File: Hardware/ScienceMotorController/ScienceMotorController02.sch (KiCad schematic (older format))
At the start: 1 part, among them U1 TM4C129E_Launchpad

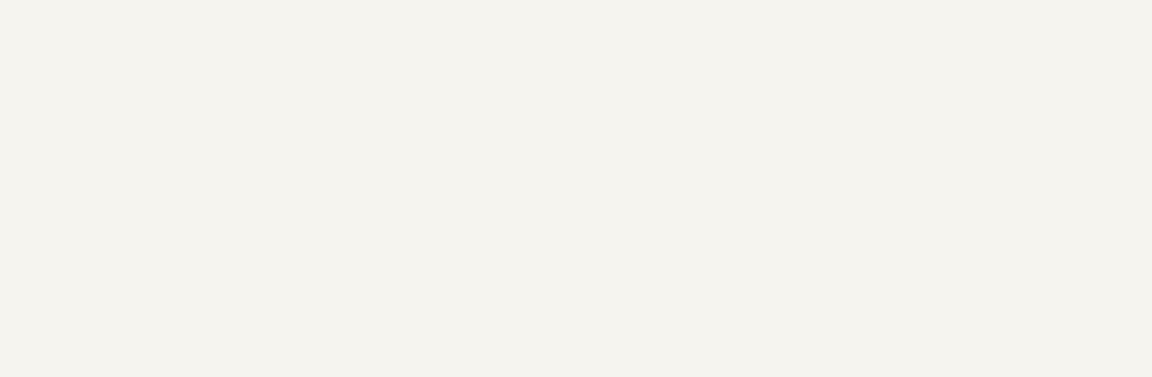
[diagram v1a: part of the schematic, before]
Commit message: Sheet titles
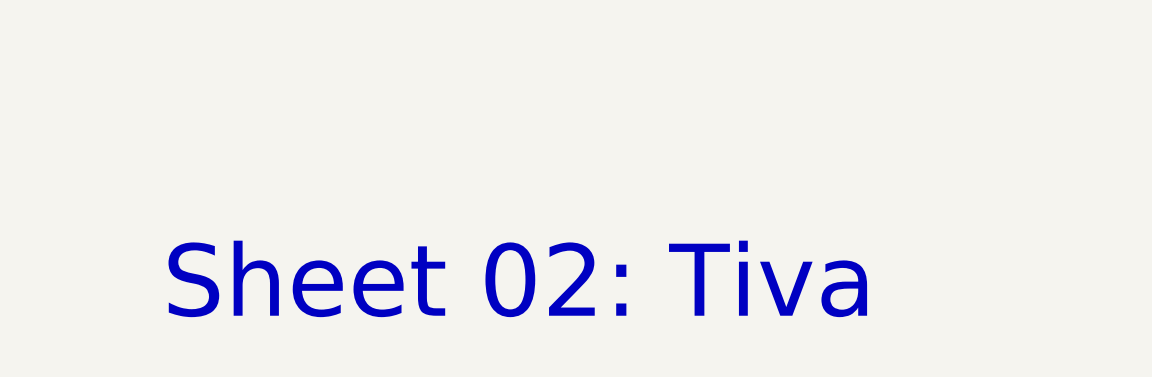
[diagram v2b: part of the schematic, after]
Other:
- note added: "Sheet 02: Tiva"
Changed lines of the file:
@@
 $Descr A4 11693 8268
 encoding utf-8
-Sheet 3 10
+Sheet 3 11
 Title ""
 Date ""
@@
 Text Notes 8450 2450 0    79   ~ 0
 PWM Pins are:\nPF_1, PF_2, PF_3, PF_0\nPG_1, PK_4, PK_5
+Text Notes 7350 7000 0    315  ~ 0
+Sheet 02: Tiva
 $EndSCHEMATC

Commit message: Flagged Tiva
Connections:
- net +3V3: now reaches U1.+3V3 (A1_1)
- net +3V3: now also U1.+3V3' (A2_1)
- net Limit_Switch_2: now reaches U1.PA6 (B1_8)
- net Limit_Switch_1: now reaches U1.PD7 (B1_7)
- net Limit_Switch_3: now reaches U1.PM4 (B1_9)
- net Limit_Switch_4: now reaches U1.PM5 (B1_10)
- net PWM_1: now reaches U1.PF1 (C1_1)
- net PWM_2: now reaches U1.PF2 (C1_2)
- net PWM_3: now reaches U1.PF3 (C1_3)
- net Current_Sense_1: now reaches U1.PB4 (B2_3)
- net Current_Sense_2: now reaches U1.PB5 (B2_4)
- net Current_Sense_3: now reaches U1.PK0 (B2_5)
- net Current_Sense_4: now reaches U1.PK1 (B2_6)
- net Current_Sense_5: now reaches U1.PK2 (B2_7)
- net Current_Sense_6: now reaches U1.PK3 (B2_8)
- net PWM_4: now reaches U1.PG1 (C2_1)
- net PWM_5: now reaches U1.PK4 (C2_2)
- net PWM_6: now reaches U1.PK5 (C2_3)
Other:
- note added: "Analog Read Pins used are:\nPB_4, PB_5, PK_0, \nPK_1, PK_2, PK_3"
- note added: "PWM Pins used are:\nPF_1, PF_2, PF_3, \nPG_1, PK_4, PK_5"
- note removed: "PWM Pins are:\nPF_1, PF_2, PF_3, PF_0\nPG_1, PK_4, PK_5"
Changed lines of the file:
@@
 U 1 1 5F715123
 P 4200 3200
-F 0 "U1" H 4300 4450 60  0000 L CNN
-F 1 "TM4C129E_Launchpad" H 3500 4350 60  0000 L CNN
+F 0 "U1" H 4300 4600 60  0000 L CNN
+F 1 "TM4C129E_Launchpad" H 3500 4500 60  0000 L CNN
 F 2 "" H 4200 3200 60  0001 C CNN
 F 3 "" H 4200 3200 60  0001 C CNN
@@
 U 2 1 5F716DA0
 P 4800 3200
-F 0 "U1" H 5000 4450 60  0000 C CNN
-F 1 "TM4C129E_Launchpad" H 4600 4350 60  0000 C CNN
+F 0 "U1" H 5000 4600 60  0000 C CNN
+F 1 "TM4C129E_Launchpad" H 4600 4500 60  0000 C CNN
 F 2 "" H 4800 3200 60  0001 C CNN
 F 3 "" H 4800 3200 60  0001 C CNN
@@
 U 3 1 5F7264AA
 P 6350 3200
-F 0 "U1" H 6450 4450 60  0000 L CNN
-F 1 "TM4C129E_Launchpad" H 5700 4350 60  0000 L CNN
+F 0 "U1" H 6450 4600 60  0000 L CNN
+F 1 "TM4C129E_Launchpad" H 5700 4500 60  0000 L CNN
 F 2 "" H 6350 3200 60  0001 C CNN
 F 3 "" H 6350 3200 60  0001 C CNN
@@
 U 4 1 5F72B226
 P 6950 3200
-F 0 "U1" H 7100 4450 60  0000 C CNN
-F 1 "TM4C129E_Launchpad" H 6700 4350 60  0000 C CNN
+F 0 "U1" H 7100 4600 60  0000 C CNN
+F 1 "TM4C129E_Launchpad" H 6700 4500 60  0000 C CNN
 F 2 "" H 6950 3200 60  0001 C CNN
 F 3 "" H 6950 3200 60  0001 C CNN
@@
 U 5 1 5F733DC7
 P 4200 4700
-F 0 "U1" H 4300 5950 60  0000 L CNN
-F 1 "TM4C129E_Launchpad" H 3500 5850 60  0000 L CNN
+F 0 "U1" H 4300 6050 60  0000 L CNN
+F 1 "TM4C129E_Launchpad" H 3500 5950 60  0000 L CNN
 F 2 "" H 4200 4700 60  0001 C CNN
 F 3 "" H 4200 4700 60  0001 C CNN
@@
 U 6 1 5F73B2DD
 P 4800 4700
-F 0 "U1" H 5000 5950 60  0000 C CNN
-F 1 "TM4C129E_Launchpad" H 4600 5850 60  0000 C CNN
+F 0 "U1" H 5000 6050 60  0000 C CNN
+F 1 "TM4C129E_Launchpad" H 4600 5950 60  0000 C CNN
 F 2 "" H 4800 4700 60  0001 C CNN
 F 3 "" H 4800 4700 60  0001 C CNN
@@
 U 7 1 5F740CF4
 P 6350 4700
-F 0 "U1" H 6450 5950 60  0000 L CNN
-F 1 "TM4C129E_Launchpad" H 5650 5850 60  0000 L CNN
+F 0 "U1" H 6450 6050 60  0000 L CNN
+F 1 "TM4C129E_Launchpad" H 5650 5950 60  0000 L CNN
 F 2 "" H 6350 4700 60  0001 C CNN
 F 3 "" H 6350 4700 60  0001 C CNN
@@
 U 8 1 5F7529E8
 P 6950 4700
-F 0 "U1" H 7100 5950 60  0000 C CNN
-F 1 "TM4C129E_Launchpad" H 6700 5850 60  0000 C CNN
+F 0 "U1" H 7100 6050 60  0000 C CNN
+F 1 "TM4C129E_Launchpad" H 6700 5950 60  0000 C CNN
 F 2 "" H 6950 4700 60  0001 C CNN
 F 3 "" H 6950 4700 60  0001 C CNN
@@
 $EndComp
 Text Notes 8450 2450 0    79   ~ 0
-PWM Pins are:\nPF_1, PF_2, PF_3, PF_0\nPG_1, PK_4, PK_5
+PWM Pins used are:\nPF_1, PF_2, PF_3, \nPG_1, PK_4, PK_5
+Text GLabel 6000 2250 0    39   Output ~ 0
+PWM_1
+Wire Wire Line
+	6000 2250 6150 2250
+Text GLabel 6000 2350 0    39   Output ~ 0
+PWM_2
+Wire Wire Line
+	6150 2350 6000 2350
+Text GLabel 6000 2450 0    39   Output ~ 0
+PWM_3
+Wire Wire Line
+	6000 2450 6150 2450
+Wire Wire Line
+	4000 2250 3850 2250
+Wire Wire Line
+	3850 2250 3850 2200
+$Comp
+L power:+3.3V #PWR?
+U 1 1 5FB06302
+P 3850 2200
+F 0 "#PWR?" H 3850 2050 50  0001 C CNN
+F 1 "+3.3V" H 3865 2373 50  0000 C CNN
+F 2 "" H 3850 2200 50  0001 C CNN
+F 3 "" H 3850 2200 50  0001 C CNN
+	1    3850 2200
+	1    0    0    -1
+$EndComp
+Text GLabel 6000 3750 0    39   Output ~ 0
+PWM_4
+Text GLabel 6000 3850 0    39   Output ~ 0
+PWM_5
+Text GLabel 6000 3950 0    39   Output ~ 0
+PWM_6
+Wire Wire Line
+	6000 3750 6150 3750
+Wire Wire Line
+	6150 3850 6000 3850
+Wire Wire Line
+	6150 3950 6000 3950
+Text Notes 8450 2950 0    79   ~ 0
+Analog Read Pins used are:\nPB_4, PB_5, PK_0, \nPK_1, PK_2, PK_3
+Text GLabel 5100 3950 2    39   Input ~ 0
+Current_Sense_1
+Wire Wire Line
+	5100 3950 5000 3950
+Wire Wire Line
+	5000 4050 5100 4050
+Wire Wire Line
+	5000 4150 5100 4150
+Wire Wire Line
+	5000 4250 5100 4250
+Wire Wire Line
+	5000 4350 5100 4350
+Wire Wire Line
+	5000 4450 5100 4450
+Text GLabel 5100 4050 2    39   Input ~ 0
+Current_Sense_2
+Text GLabel 5100 4150 2    39   Input ~ 0
+Current_Sense_3
+Text GLabel 5100 4250 2    39   Input ~ 0
+Current_Sense_4
+Text GLabel 5100 4350 2    39   Input ~ 0
+Current_Sense_5
+Text GLabel 5100 4450 2    39   Input ~ 0
+Current_Sense_6
+$Comp
+L power:+3.3V #PWR?
+U 1 1 5FB0EFA7
+P 3850 3700
+F 0 "#PWR?" H 3850 3550 50  0001 C CNN
+F 1 "+3.3V" H 3865 3873 50  0000 C CNN
+F 2 "" H 3850 3700 50  0001 C CNN
+F 3 "" H 3850 3700 50  0001 C CNN
+	1    3850 3700
+	1    0    0    -1
+$EndComp
+Wire Wire Line
+	3850 3700 3850 3750
+Wire Wire Line
+	3850 3750 4000 3750
+Text GLabel 5100 2850 2    39   Input ~ 0
+Limit_Switch_1
+Wire Wire Line
+	5100 2850 5000 2850
+Text GLabel 5100 2950 2    39   Input ~ 0
+Limit_Switch_2
+Text GLabel 5100 3050 2    39   Input ~ 0
+Limit_Switch_3
+Text GLabel 5100 3150 2    39   Input ~ 0
+Limit_Switch_4
+Wire Wire Line
+	5100 2950 5000 2950
+Wire Wire Line
+	5000 3050 5100 3050
+Wire Wire Line
+	5100 3150 5000 3150
 Text Notes 7350 7000 0    315  ~ 0
 Sheet 02: Tiva

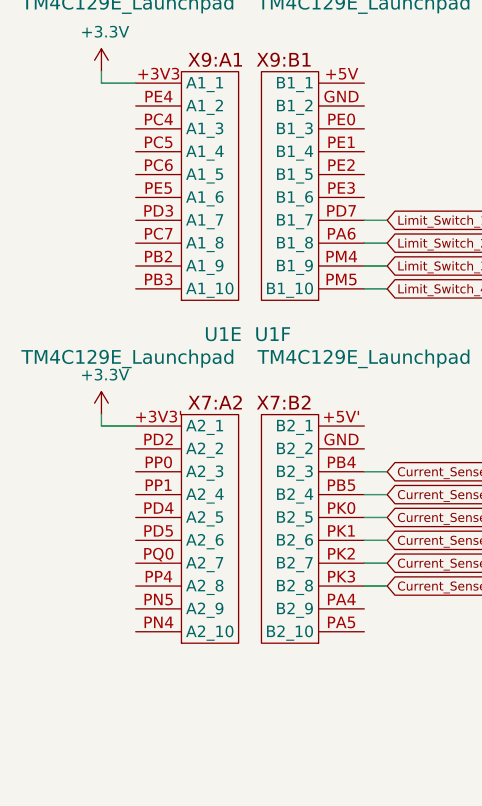
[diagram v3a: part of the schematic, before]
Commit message: changed everything to actuation, added schottky diode, added A/B flags to tiva
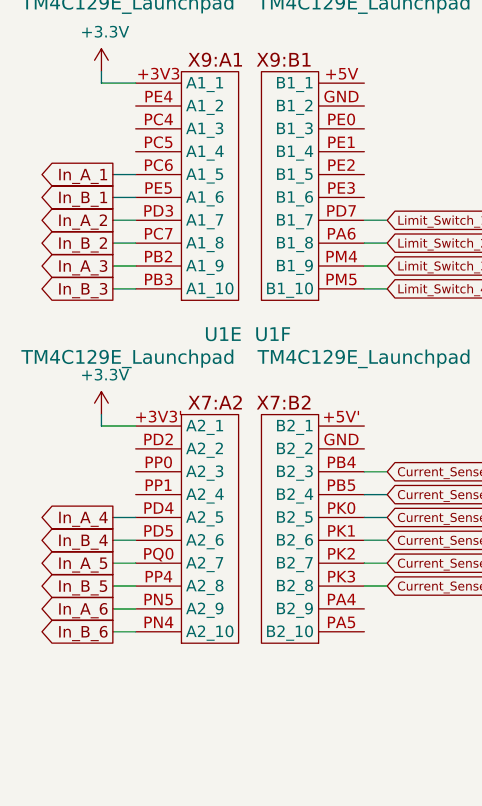
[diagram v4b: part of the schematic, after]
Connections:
- net In_A_3: now reaches U1.PB2 (A1_9)
- net In_B_3: now reaches U1.PB3 (A1_10)
- net In_A_1: now reaches U1.PC6 (A1_5)
- net In_B_2: now reaches U1.PC7 (A1_8)
- net In_A_2: now reaches U1.PD3 (A1_7)
- net In_B_1: now reaches U1.PE5 (A1_6)
- net In_A_4: now reaches U1.PD4 (A2_5)
- net In_B_4: now reaches U1.PD5 (A2_6)
- net In_B_6: now reaches U1.PN4 (A2_10)
- net In_A_6: now reaches U1.PN5 (A2_9)
- net In_B_5: now reaches U1.PP4 (A2_8)
- net In_A_5: now reaches U1.PQ0 (A2_7)
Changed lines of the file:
@@
 Text Notes 7350 7000 0    315  ~ 0
 Sheet 02: Tiva
+Text GLabel 3900 2650 0    50   Output ~ 0
+In_A_1
+Wire Wire Line
+	4000 2650 3900 2650
+Text GLabel 3900 2750 0    50   Output ~ 0
+In_B_1
+Wire Wire Line
+	4000 2750 3900 2750
+Text GLabel 3900 2850 0    50   Output ~ 0
+In_A_2
+Text GLabel 3900 2950 0    50   Output ~ 0
+In_B_2
+Text GLabel 3900 3050 0    50   Output ~ 0
+In_A_3
+Text GLabel 3900 4150 0    50   Output ~ 0
+In_A_4
+Text GLabel 3900 3150 0    50   Output ~ 0
+In_B_3
+Text GLabel 3900 4250 0    50   Output ~ 0
+In_B_4
+Text GLabel 3900 4350 0    50   Output ~ 0
+In_A_5
+Text GLabel 3900 4450 0    50   Output ~ 0
+In_B_5
+Text GLabel 3900 4550 0    50   Output ~ 0
+In_A_6
+Text GLabel 3900 4650 0    50   Output ~ 0
+In_B_6
+Wire Wire Line
+	4000 2850 3900 2850
+Wire Wire Line
+	3900 2950 4000 2950
+Wire Wire Line
+	4000 3050 3900 3050
+Wire Wire Line
+	4000 3150 3900 3150
+Wire Wire Line
+	3900 4150 4000 4150
+Wire Wire Line
+	4000 4250 3900 4250
+Wire Wire Line
+	3900 4350 4000 4350
+Wire Wire Line
+	4000 4450 3900 4450
+Wire Wire Line
+	3900 4550 4000 4550
+Wire Wire Line
+	4000 4650 3900 4650
 $EndSCHEMATC

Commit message: added ferrite beads
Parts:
- added D?: Yellow, symbol Device:LED
- added D?: Red, symbol Device:LED
- added R? (x2): 330, symbol Device:R
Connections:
- net at U1.PM6 (D2_10): now also R?.1
- net at U1.PP3 (D2_8): now also R?.1
- net +3V3 renamed +3.3VA
- new net: D?.2 (A), R?.2 (x2)
- new net GND: D?.1 (K), D?.1 (K)
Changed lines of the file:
@@
 Wire Wire Line
 	3850 2250 3850 2200
-$Comp
-L power:+3.3V #PWR?
-U 1 1 5FB06302
-P 3850 2200
-F 0 "#PWR?" H 3850 2050 50  0001 C CNN
-F 1 "+3.3V" H 3865 2373 50  0000 C CNN
-F 2 "" H 3850 2200 50  0001 C CNN
-F 3 "" H 3850 2200 50  0001 C CNN
-	1    3850 2200
-	1    0    0    -1
-$EndComp
 Text GLabel 6000 3750 0    39   Output ~ 0
 PWM_4
@@
 Text GLabel 5100 4450 2    39   Input ~ 0
 Current_Sense_6
-$Comp
-L power:+3.3V #PWR?
-U 1 1 5FB0EFA7
-P 3850 3700
-F 0 "#PWR?" H 3850 3550 50  0001 C CNN
-F 1 "+3.3V" H 3865 3873 50  0000 C CNN
-F 2 "" H 3850 3700 50  0001 C CNN
-F 3 "" H 3850 3700 50  0001 C CNN
-	1    3850 3700
-	1    0    0    -1
-$EndComp
 Wire Wire Line
 	3850 3700 3850 3750
@@
 Wire Wire Line
 	4000 4650 3900 4650
+$Comp
+L power:+3.3VA #PWR?
+U 1 1 5F8320C1
+P 3850 2200
+F 0 "#PWR?" H 3850 2050 50  0001 C CNN
+F 1 "+3.3VA" H 3865 2373 50  0000 C CNN
+F 2 "" H 3850 2200 50  0001 C CNN
+F 3 "" H 3850 2200 50  0001 C CNN
+	1    3850 2200
+	1    0    0    -1
+$EndComp
+$Comp
+L power:+3.3VA #PWR?
+U 1 1 5F833369
+P 3850 3700
+F 0 "#PWR?" H 3850 3550 50  0001 C CNN
+F 1 "+3.3VA" H 3865 3873 50  0000 C CNN
+F 2 "" H 3850 3700 50  0001 C CNN
+F 3 "" H 3850 3700 50  0001 C CNN
+	1    3850 3700
+	1    0    0    -1
+$EndComp
+Wire Wire Line
+	7150 4650 7250 4650
+$Comp
+L Device:R R?
+U 1 1 5F836CF2
+P 7400 4650
+F 0 "R?" V 7300 4650 50  0000 C CNN
+F 1 "330" V 7400 4650 50  0000 C CNN
+F 2 "" V 7330 4650 50  0001 C CNN
+F 3 "~" H 7400 4650 50  0001 C CNN
+	1    7400 4650
+	0    -1   -1   0
+$EndComp
+$Comp
+L Device:LED D?
+U 1 1 5F838880
+P 7800 4650
+F 0 "D?" H 7800 4750 50  0000 C CNN
+F 1 "Yellow" H 7600 4700 50  0000 C CNN
+F 2 "" H 7800 4650 50  0001 C CNN
+F 3 "~" H 7800 4650 50  0001 C CNN
+	1    7800 4650
+	-1   0    0    1
+$EndComp
+Wire Wire Line
+	7550 4650 7650 4650
+Wire Wire Line
+	7950 4650 8250 4650
+$Comp
+L power:GND #PWR?
+U 1 1 5F83BC3E
+P 8250 4650
+F 0 "#PWR?" H 8250 4400 50  0001 C CNN
+F 1 "GND" V 8255 4522 50  0000 R CNN
+F 2 "" H 8250 4650 50  0001 C CNN
+F 3 "" H 8250 4650 50  0001 C CNN
+	1    8250 4650
+	0    -1   -1   0
+$EndComp
+$Comp
+L Device:R R?
+U 1 1 5F83D1F8
+P 7400 4450
+F 0 "R?" V 7300 4450 50  0000 C CNN
+F 1 "330" V 7400 4450 50  0000 C CNN
+F 2 "" V 7330 4450 50  0001 C CNN
+F 3 "~" H 7400 4450 50  0001 C CNN
+	1    7400 4450
+	0    -1   -1   0
+$EndComp
+$Comp
+L Device:LED D?
+U 1 1 5F83D4EA
+P 7800 4450
+F 0 "D?" H 7800 4550 50  0000 C CNN
+F 1 "Red" H 7650 4500 50  0000 C CNN
+F 2 "" H 7800 4450 50  0001 C CNN
+F 3 "~" H 7800 4450 50  0001 C CNN
+	1    7800 4450
+	-1   0    0    1
+$EndComp
+$Comp
+L power:GND #PWR?
+U 1 1 5F83E3D5
+P 8250 4450
+F 0 "#PWR?" H 8250 4200 50  0001 C CNN
+F 1 "GND" V 8255 4322 50  0000 R CNN
+F 2 "" H 8250 4450 50  0001 C CNN
+F 3 "" H 8250 4450 50  0001 C CNN
+	1    8250 4450
+	0    -1   -1   0
+$EndComp
+Wire Wire Line
+	8250 4450 7950 4450
+Wire Wire Line
+	7650 4450 7550 4450
+Wire Wire Line
+	7250 4450 7150 4450
 $EndSCHEMATC

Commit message: schematic review
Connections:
- net GND: now also U1.GND (B1_2), U1.GND (B2_2), U1.GND (D1_1), U1.GND (D2_1)
- net +3.3VA renamed 3.3VA
- no-connect marks 0 -> 44
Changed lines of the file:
@@
 $Descr A4 11693 8268
 encoding utf-8
-Sheet 3 11
+Sheet 3 10
 Title ""
 Date ""
@@
 U 1 1 5F715123
 P 4200 3200
-F 0 "U1" H 4300 4600 60  0000 L CNN
-F 1 "TM4C129E_Launchpad" H 3500 4500 60  0000 L CNN
+F 0 "U1" H 4300 4700 60  0000 L CNN
+F 1 "TM4C129E_Launchpad" H 3500 4600 60  0000 L CNN
 F 2 "" H 4200 3200 60  0001 C CNN
 F 3 "" H 4200 3200 60  0001 C CNN
@@
 U 2 1 5F716DA0
 P 4800 3200
-F 0 "U1" H 5000 4600 60  0000 C CNN
-F 1 "TM4C129E_Launchpad" H 4600 4500 60  0000 C CNN
+F 0 "U1" H 5000 4700 60  0000 C CNN
+F 1 "TM4C129E_Launchpad" H 4600 4600 60  0000 C CNN
 F 2 "" H 4800 3200 60  0001 C CNN
 F 3 "" H 4800 3200 60  0001 C CNN
@@
 U 5 1 5F733DC7
 P 4200 4700
-F 0 "U1" H 4300 6050 60  0000 L CNN
-F 1 "TM4C129E_Launchpad" H 3500 5950 60  0000 L CNN
+F 0 "U1" H 4300 6100 60  0000 L CNN
+F 1 "TM4C129E_Launchpad" H 3500 6000 60  0000 L CNN
 F 2 "" H 4200 4700 60  0001 C CNN
 F 3 "" H 4200 4700 60  0001 C CNN
@@
 U 6 1 5F73B2DD
 P 4800 4700
-F 0 "U1" H 5000 6050 60  0000 C CNN
-F 1 "TM4C129E_Launchpad" H 4600 5950 60  0000 C CNN
+F 0 "U1" H 5000 6100 60  0000 C CNN
+F 1 "TM4C129E_Launchpad" H 4600 6000 60  0000 C CNN
 F 2 "" H 4800 4700 60  0001 C CNN
 F 3 "" H 4800 4700 60  0001 C CNN
@@
 Text GLabel 5100 4450 2    39   Input ~ 0
 Current_Sense_6
-Wire Wire Line
-	3850 3700 3850 3750
-Wire Wire Line
-	3850 3750 4000 3750
 Text GLabel 5100 2850 2    39   Input ~ 0
 Limit_Switch_1
@@
 Wire Wire Line
 	4000 4650 3900 4650
-$Comp
-L power:+3.3VA #PWR?
-U 1 1 5F8320C1
-P 3850 2200
-F 0 "#PWR?" H 3850 2050 50  0001 C CNN
-F 1 "+3.3VA" H 3865 2373 50  0000 C CNN
-F 2 "" H 3850 2200 50  0001 C CNN
-F 3 "" H 3850 2200 50  0001 C CNN
-	1    3850 2200
-	1    0    0    -1
-$EndComp
-$Comp
-L power:+3.3VA #PWR?
-U 1 1 5F833369
-P 3850 3700
-F 0 "#PWR?" H 3850 3550 50  0001 C CNN
-F 1 "+3.3VA" H 3865 3873 50  0000 C CNN
-F 2 "" H 3850 3700 50  0001 C CNN
-F 3 "" H 3850 3700 50  0001 C CNN
-	1    3850 3700
-	1    0    0    -1
-$EndComp
 Wire Wire Line
 	7150 4650 7250 4650
@@
 Wire Wire Line
 	7550 4650 7650 4650
-Wire Wire Line
-	7950 4650 8250 4650
 $Comp
 L power:GND #PWR?
 U 1 1 5F83BC3E
-P 8250 4650
-F 0 "#PWR?" H 8250 4400 50  0001 C CNN
-F 1 "GND" V 8255 4522 50  0000 R CNN
-F 2 "" H 8250 4650 50  0001 C CNN
-F 3 "" H 8250 4650 50  0001 C CNN
-	1    8250 4650
-	0    -1   -1   0
+P 8300 4700
+F 0 "#PWR?" H 8300 4450 50  0001 C CNN
+F 1 "GND" H 8550 4650 50  0000 R CNN
+F 2 "" H 8300 4700 50  0001 C CNN
+F 3 "" H 8300 4700 50  0001 C CNN
+	1    8300 4700
+	1    0    0    -1
 $EndComp
 $Comp
@@
 L power:GND #PWR?
 U 1 1 5F83E3D5
-P 8250 4450
-F 0 "#PWR?" H 8250 4200 50  0001 C CNN
-F 1 "GND" V 8255 4322 50  0000 R CNN
-F 2 "" H 8250 4450 50  0001 C CNN
-F 3 "" H 8250 4450 50  0001 C CNN
-	1    8250 4450
-	0    -1   -1   0
-$EndComp
-Wire Wire Line
-	8250 4450 7950 4450
+P 8300 4500
+F 0 "#PWR?" H 8300 4250 50  0001 C CNN
+F 1 "GND" H 8550 4450 50  0000 R CNN
+F 2 "" H 8300 4500 50  0001 C CNN
+F 3 "" H 8300 4500 50  0001 C CNN
+	1    8300 4500
+	1    0    0    -1
+$EndComp
 Wire Wire Line
 	7650 4450 7550 4450
 Wire Wire Line
 	7250 4450 7150 4450
+Wire Wire Line
+	8300 4450 8300 4500
+Wire Wire Line
+	7950 4450 8300 4450
+Wire Wire Line
+	8300 4650 8300 4700
+Wire Wire Line
+	7950 4650 8300 4650
+NoConn ~ 7150 3850
+NoConn ~ 7150 3950
+NoConn ~ 7150 4050
+NoConn ~ 7150 4150
+NoConn ~ 7150 4250
+NoConn ~ 7150 4350
+NoConn ~ 7150 4550
+NoConn ~ 6150 4650
+NoConn ~ 6150 4550
+NoConn ~ 6150 4450
+NoConn ~ 6150 4350
+NoConn ~ 6150 4250
+NoConn ~ 6150 4150
+NoConn ~ 6150 4050
+Wire Wire Line
+	7150 3750 7350 3750
+Wire Wire Line
+	7350 3750 7350 3800
+$Comp
+L power:GND #PWR?
+U 1 1 5F8BF81D
+P 7350 3800
+F 0 "#PWR?" H 7350 3550 50  0001 C CNN
+F 1 "GND" H 7600 3750 50  0000 R CNN
+F 2 "" H 7350 3800 50  0001 C CNN
+F 3 "" H 7350 3800 50  0001 C CNN
+	1    7350 3800
+	1    0    0    -1
+$EndComp
+NoConn ~ 4000 3850
+NoConn ~ 4000 3950
+NoConn ~ 4000 4050
+Wire Wire Line
+	5000 3850 5700 3850
+Wire Wire Line
+	5700 3850 5700 3950
+$Comp
+L power:GND #PWR?
+U 1 1 5F8C3C62
+P 5700 3950
+F 0 "#PWR?" H 5700 3700 50  0001 C CNN
+F 1 "GND" H 5800 3800 50  0000 R CNN
+F 2 "" H 5700 3950 50  0001 C CNN
+F 3 "" H 5700 3950 50  0001 C CNN
+	1    5700 3950
+	1    0    0    -1
+$EndComp
+NoConn ~ 5000 4550
+NoConn ~ 5000 4650
+NoConn ~ 5000 2750
+NoConn ~ 5000 2650
+NoConn ~ 5000 2550
+NoConn ~ 5000 2450
+NoConn ~ 4000 2550
+NoConn ~ 4000 2450
+NoConn ~ 4000 2350
+NoConn ~ 6150 2550
+NoConn ~ 6150 2650
+NoConn ~ 6150 2750
+NoConn ~ 6150 2850
+NoConn ~ 6150 2950
+NoConn ~ 6150 3050
+NoConn ~ 6150 3150
+NoConn ~ 7150 3150
+NoConn ~ 7150 3050
+NoConn ~ 7150 2950
+NoConn ~ 7150 2850
+NoConn ~ 7150 2750
+NoConn ~ 7150 2650
+NoConn ~ 7150 2550
+NoConn ~ 7150 2450
+NoConn ~ 7150 2350
+Wire Wire Line
+	7150 2250 7400 2250
+Wire Wire Line
+	7400 2250 7400 2300
+$Comp
+L power:GND #PWR?
+U 1 1 5F8D9D39
+P 7400 2300
+F 0 "#PWR?" H 7400 2050 50  0001 C CNN
+F 1 "GND" H 7500 2150 50  0000 R CNN
+F 2 "" H 7400 2300 50  0001 C CNN
+F 3 "" H 7400 2300 50  0001 C CNN
+	1    7400 2300
+	1    0    0    -1
+$EndComp
+Wire Wire Line
+	5000 2350 5250 2350
+Wire Wire Line
+	5250 2350 5250 2400
+$Comp
+L power:GND #PWR?
+U 1 1 5F8DBCE3
+P 5250 2400
+F 0 "#PWR?" H 5250 2150 50  0001 C CNN
+F 1 "GND" H 5350 2250 50  0000 R CNN
+F 2 "" H 5250 2400 50  0001 C CNN
+F 3 "" H 5250 2400 50  0001 C CNN
+	1    5250 2400
+	1    0    0    -1
+$EndComp
+NoConn ~ 5000 2250
+NoConn ~ 5000 3750
+Text HLabel 3850 2200 1    50   Input ~ 0
+3.3VA
+Text HLabel 3750 3750 0    50   Input ~ 0
+3.3VA
+Wire Wire Line
+	3750 3750 4000 3750
 $EndSCHEMATC

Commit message: made some more hierarchal changes
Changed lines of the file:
@@
 Wire Wire Line
 	6000 2450 6150 2450
-Wire Wire Line
-	4000 2250 3850 2250
-Wire Wire Line
-	3850 2250 3850 2200
 Text GLabel 6000 3750 0    39   Output ~ 0
 PWM_4
@@
 NoConn ~ 5000 2250
 NoConn ~ 5000 3750
-Text HLabel 3850 2200 1    50   Input ~ 0
+Text HLabel 3750 2250 0    50   Input ~ 0
 3.3VA
 Text HLabel 3750 3750 0    50   Input ~ 0
@@
 Wire Wire Line
 	3750 3750 4000 3750
+Wire Wire Line
+	3750 2250 4000 2250
 $EndSCHEMATC

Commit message: fixed hierarchical
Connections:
- net Current_Sense_1 renamed sheet5FA34ACC/Current_Sense_1
- net Current_Sense_2 renamed sheet5FA34ACD/Current_Sense_2
- net Current_Sense_3 renamed sheet5FA34ACE/Current_Sense_3
- net Current_Sense_4 renamed sheet5FA34ACF/Current_Sense_4
- net Current_Sense_5 renamed sheet5FA34AD0/Current_Sense_5
- net Current_Sense_6 renamed sheet5FA34AD1/Current_Sense_6
- net In_A_1 renamed sheet5FA34ACC/In_A_1
- net In_A_2 renamed sheet5FA34ACD/In_A_2
- net In_A_3 renamed sheet5FA34ACE/In_A_3
- net In_A_4 renamed sheet5FA34ACF/In_A_4
- net In_A_5 renamed sheet5FA34AD0/In_A_5
- net In_A_6 renamed sheet5FA34AD1/In_A_6
- net In_B_1 renamed sheet5FA34ACC/In_B_1
- net In_B_2 renamed sheet5FA34ACD/In_B_2
- net In_B_3 renamed sheet5FA34ACE/In_B_3
- net In_B_4 renamed sheet5FA34ACF/In_B_4
- net In_B_5 renamed sheet5FA34AD0/In_B_5
- net In_B_6 renamed sheet5FA34AD1/In_B_6
- net Limit_Switch_1 renamed sheet5FC42AEB/Limit_Switch_1
- net Limit_Switch_2 renamed sheet5FC42AEB/Limit_Switch_2
- net Limit_Switch_3 renamed sheet5FC42AEB/Limit_Switch_3
- net Limit_Switch_4 renamed sheet5FC42AEB/Limit_Switch_4
- net PWM_1 renamed sheet5FA34ACC/PWM_1
- net PWM_2 renamed sheet5FA34ACD/PWM_2
- net PWM_3 renamed sheet5FA34ACE/PWM_3
- net PWM_4 renamed sheet5FA34ACF/PWM_4
- net PWM_5 renamed sheet5FA34AD0/PWM_5
- net PWM_6 renamed sheet5FA34AD1/PWM_6
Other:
- moved on the sheet: D?, R?, U1A, U1B, U1C, U1D, U1E, U1F, U1G, U1H
